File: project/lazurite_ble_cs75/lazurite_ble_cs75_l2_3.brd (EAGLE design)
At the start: 54 x 28.9 mm, 11 parts

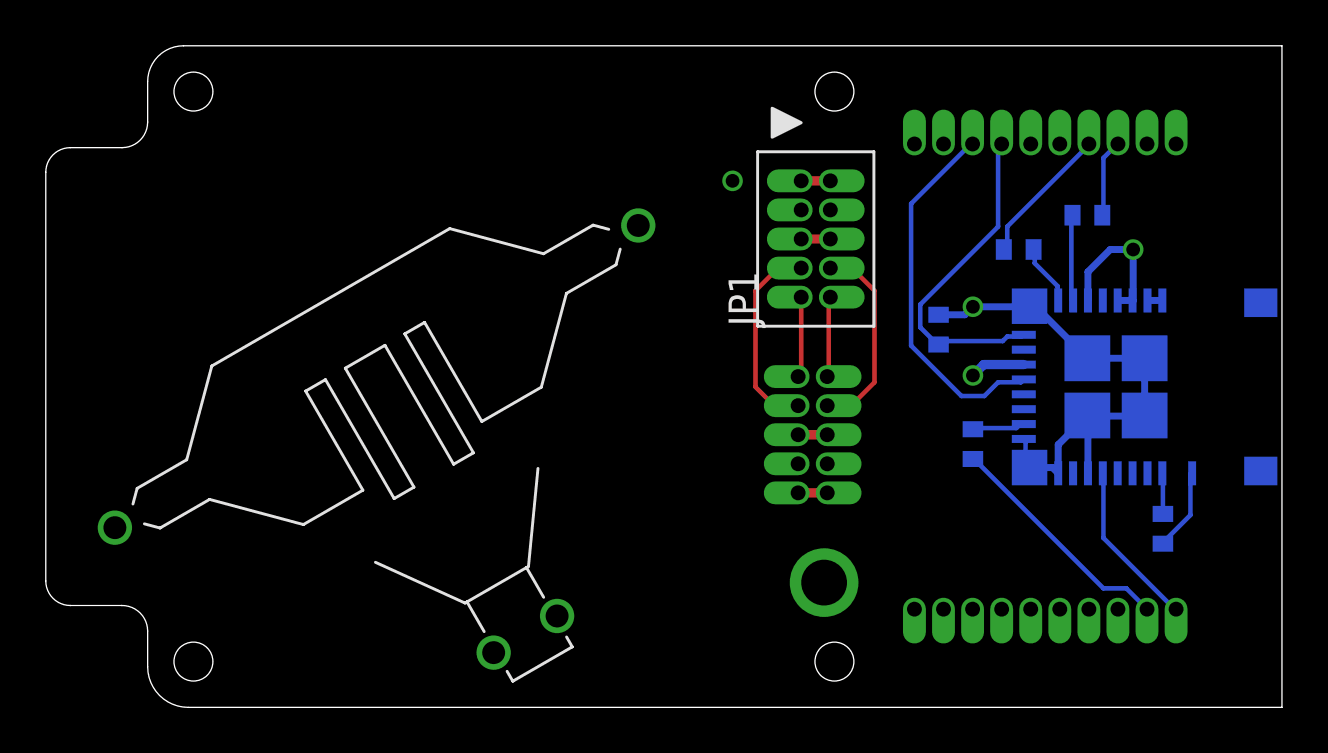
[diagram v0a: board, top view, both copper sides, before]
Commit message: update libraries and all schematic/board data.
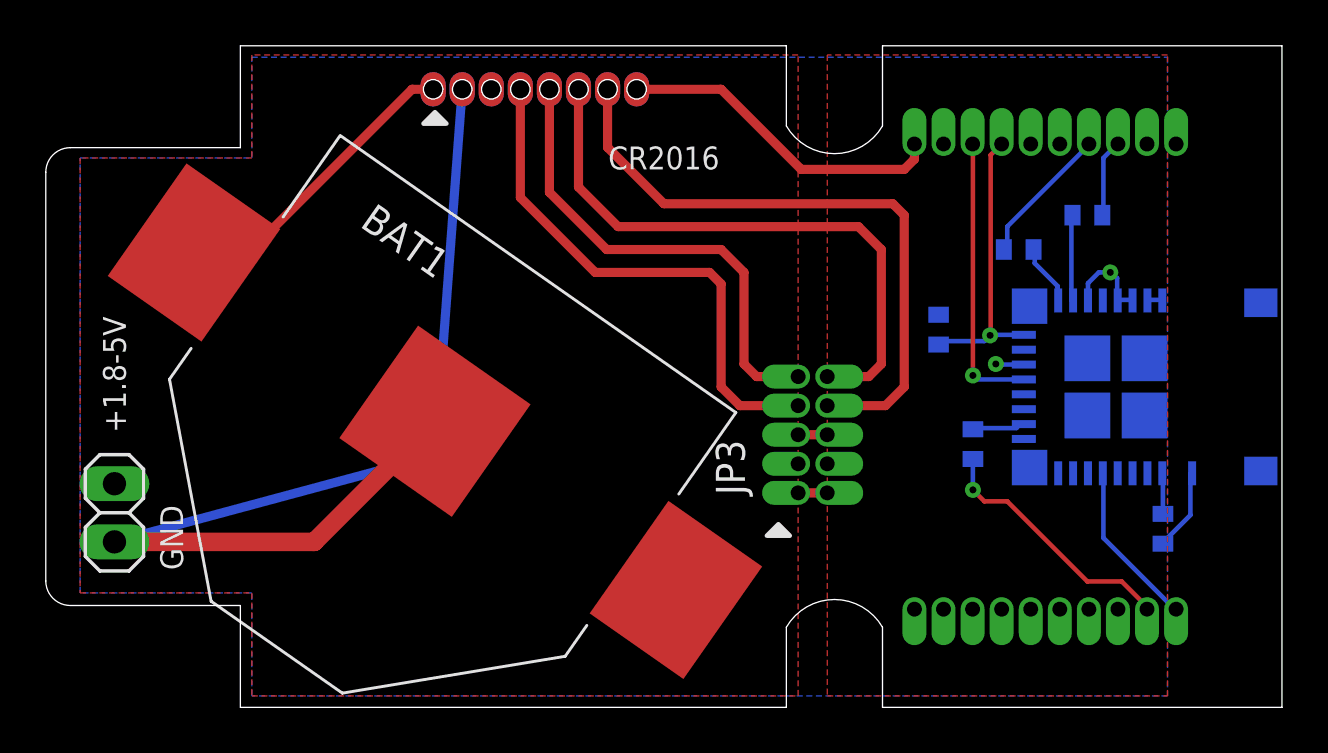
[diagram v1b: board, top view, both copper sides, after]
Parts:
- added BAT1: BK-5067, lz-shield:BK-5067
- JP1: value PINHD_2X5_HALF -> (none); device lazurite:PINHD_2X5_HALF -> pinhead:1X02
- U$1: value TAKACHI_CS75_BATTERY -> XB-1-X; device lz-shield:TAKACHI_CS75_BATTERY -> lz-shield:XB-1-X
- moved JP1 33.3 mm to (3.00, 8.50), turned to 270 degrees
- moved U$1 14.6 mm to (22.0, 27.0), turned to 0 degrees
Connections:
- net +3V3: now also U$1.8_1; no longer JP1.4, JP1.5
- net +5V: now also BAT1.VDD1, BAT1.VDD2, U$1.1_1; no longer JP1.0, U$1.P1, U$1.P2
- net 0: now also U$1.6_1; no longer JP1.9
- net 1: now also U$1.5_1; no longer JP1.8
- net GND: now also BAT1.GND, U$1.2_2; no longer JP1.3, U$1.N1, U$1.N2
- net TEST0: now also U$1.7_1; no longer JP1.7
- net TEST1N: now also U$1.4_1; no longer JP1.6
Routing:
- net GND: track 23.4 -> 46.7 mm, vias 2 -> 0
- net 0: track 3.50 -> 26.2 mm
- net TEST0: track 8.84 -> 27.9 mm
- net 1: track 3.52 -> 21.0 mm
- net TEST1N: track 8.92 -> 23.3 mm
- net +5V: track 2.54 -> 14.7 mm, vias 1 -> 0
- net +3V3: track 12.1 -> 20.9 mm
- net CTS: track 16.1 -> 12.4 mm, vias 0 -> 1
- net RTS: track 14.7 -> 12.7 mm, vias 0 -> 1
- net N$7: track 10.3 -> 11.2 mm, vias 0 -> 1
- added copper zone on layer 1, net +3V3
- added copper zone on layer 1, net +5V
- added copper zone on layer 16, net GND
- removed copper zone on layer 2, net +3V3
- removed copper zone on layer 2, net +5V
- removed copper zone on layer 3, net GND
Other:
- outline, holes or cut-outs redrawn
- board text added: "+1.8-5V"
- board text added: "CR2016"
- board text added: "Designed in Japan Made in Japan"
- board text added: "GND"
- board text added: "Lazurite 920J BLE Shiled"
- board text added: "http://www.lapis-semi.com/lazurite-jp/"
